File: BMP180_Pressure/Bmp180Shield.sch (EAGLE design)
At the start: 5 parts

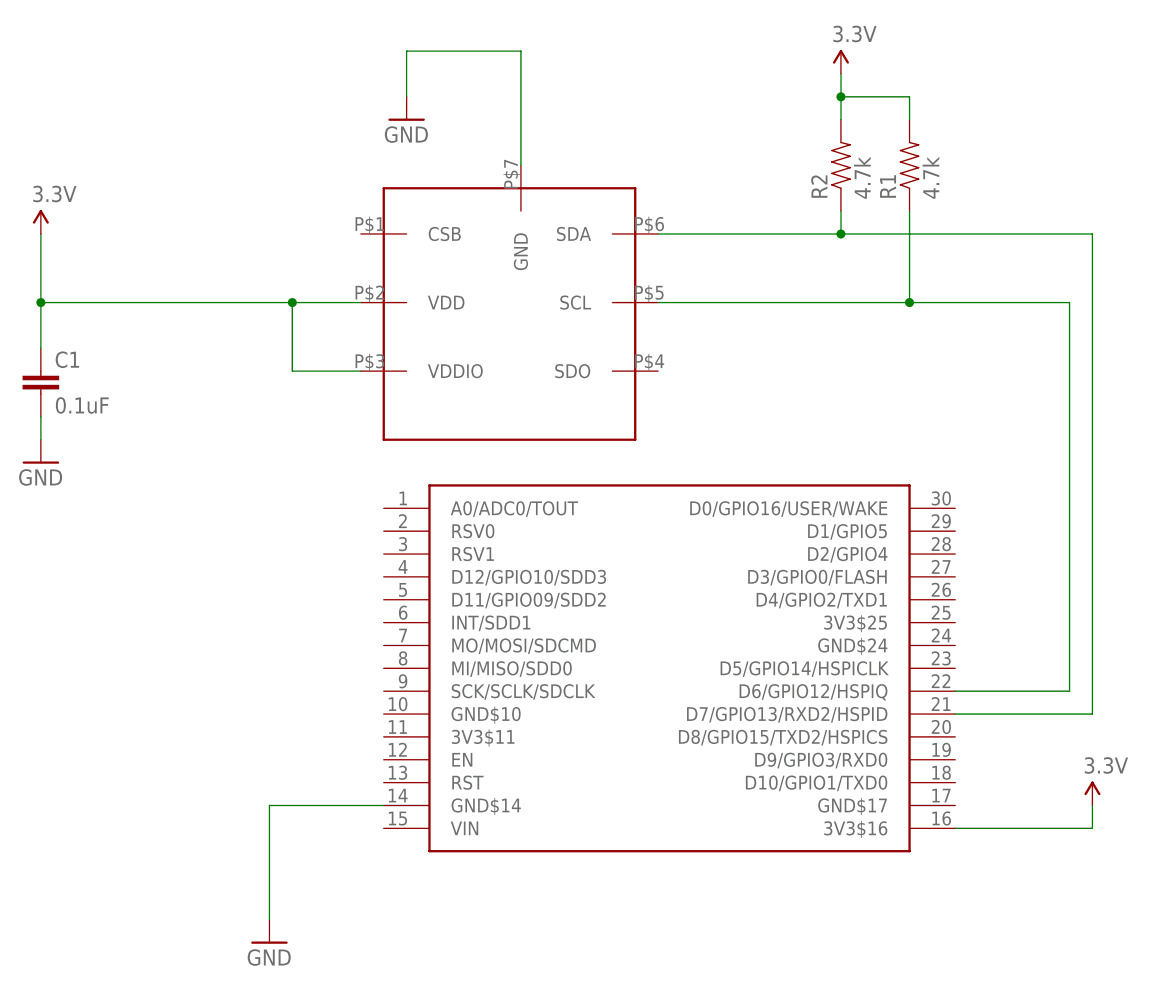
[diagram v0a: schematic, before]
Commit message: Updated BMP180 symbol Removed BMP085 shield (redundant) Added DS3231 RTC Shield Added LTC2495 ADC Shield Added chip data sheets for each shield
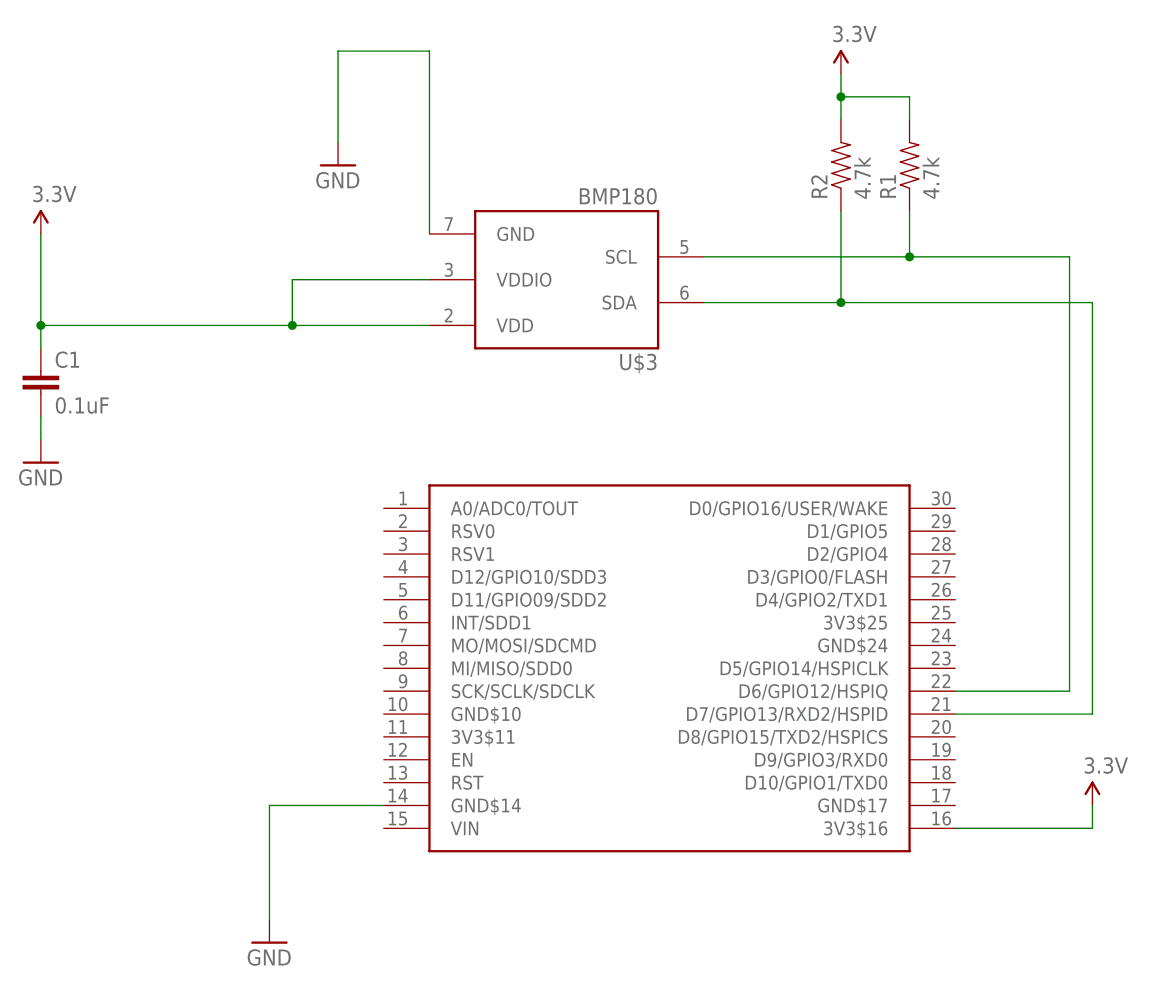
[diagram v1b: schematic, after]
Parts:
- U$3: device NerduinoShieldLib:BMP180 -> SparkFun-Sensors:BMP180
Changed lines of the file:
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@@
 <?xml version="1.0" encoding="utf-8"?>
 <!DOCTYPE eagle SYSTEM "eagle.dtd">
-<eagle version="7.3.0">
+<eagle version="7.4.0">
 <drawing>
 <settings>
@@
 <layer number="54" name="bGND_GNDA" color="1" fill="9" visible="no" active="no"/>
 <layer number="56" name="wert" color="7" fill="1" visible="no" active="no"/>
+<layer number="57" name="tCAD" color="7" fill="1" visible="no" active="no"/>
+<layer number="59" name="tCarbon" color="7" fill="1" visible="no" active="no"/>
+<layer number="60" name="bCarbon" color="7" fill="1" visible="no" active="no"/>
 <layer number="90" name="Modules" color="5" fill="1" visible="yes" active="yes"/>
 <layer number="91" name="Nets" color="2" fill="1" visible="yes" active="yes"/>
@@
 <layer number="97" name="Info" color="7" fill="1" visible="yes" active="yes"/>
 <layer number="98" name="Guide" color="6" fill="1" visible="yes" active="yes"/>
+<layer number="99" name="SpiceOrder" color="7" fill="1" visible="yes" active="yes"/>
 <layer number="100" name="Muster" color="7" fill="1" visible="no" active="no"/>
 <layer number="101" name="Patch_Top" color="12" fill="4" visible="yes" active="yes"/>
@@
 <layer number="106" name="bPlate" color="7" fill="1" visible="yes" active="yes"/>
 <layer number="107" name="Crop" color="7" fill="1" visible="yes" active="yes"/>
+<layer number="108" name="tplace-old" color="10" fill="1" visible="yes" active="yes"/>
+<layer number="109" name="ref-old" color="11" fill="1" visible="yes" active="yes"/>
+<layer number="110" name="fp0" color="7" fill="1" visible="yes" active="yes"/>
+<layer number="111" name="LPC17xx" color="7" fill="1" visible="yes" active="yes"/>
+<layer number="112" name="tSilk" color="7" fill="1" visible="yes" active="yes"/>
+<layer number="113" name="IDFDebug" color="7" fill="1" visible="yes" active="yes"/>
 <layer number="116" name="Patch_BOT" color="9" fill="4" visible="yes" active="yes"/>
+<layer number="118" name="Rect_Pads" color="7" fill="1" visible="yes" active="yes"/>
 <layer number="121" name="_tsilk" color="7" fill="1" visible="yes" active="yes"/>
 <layer number="122" name="_bsilk" color="7" fill="1" visible="yes" active="yes"/>
+<layer number="123" name="tTestmark" color="7" fill="1" visible="yes" active="yes"/>
+<layer number="124" name="bTestmark" color="7" fill="1" visible="yes" active="yes"/>
 <layer number="125" name="_tNames" color="7" fill="1" visible="yes" active="yes"/>
+<layer number="126" name="_bNames" color="7" fill="1" visible="yes" active="yes"/>
+<layer number="127" name="_tValues" color="7" fill="1" visible="yes" active="yes"/>
+<layer number="128" name="_bValues" color="7" fill="1" visible="yes" active="yes"/>
+<layer number="129" name="Mask" color="7" fill="1" visible="yes" active="yes"/>
+<layer number="131" name="tAdjust" color="7" fill="1" visible="yes" active="yes"/>
+<layer number="132" name="bAdjust" color="7" fill="1" visible="yes" active="yes"/>
 <layer number="144" name="Drill_legend" color="7" fill="1" visible="yes" active="yes"/>
+<layer number="150" name="Notes" color="7" fill="1" visible="yes" active="yes"/>
 <layer number="151" name="HeatSink" color="7" fill="1" visible="yes" active="yes"/>
+<layer number="152" name="_bDocu" color="7" fill="1" visible="yes" active="yes"/>
+<layer number="153" name="FabDoc1" color="7" fill="1" visible="yes" active="yes"/>
+<layer number="154" name="FabDoc2" color="7" fill="1" visible="yes" active="yes"/>
+<layer number="155" name="FabDoc3" color="7" fill="1" visible="yes" active="yes"/>
+<layer number="199" name="Contour" color="7" fill="1" visible="yes" active="yes"/>
 <layer number="200" name="200bmp" color="1" fill="10" visible="yes" active="yes"/>
 <layer number="201" name="201bmp" color="2" fill="10" visible="yes" active="yes"/>
@@
 <layer number="223" name="223bmp" color="24" fill="1" visible="no" active="no"/>
 <layer number="224" name="224bmp" color="25" fill="1" visible="no" active="no"/>
+<layer number="225" name="225bmp" color="7" fill="1" visible="yes" active="yes"/>
+<layer number="226" name="226bmp" color="7" fill="1" visible="yes" active="yes"/>
+<layer number="227" name="227bmp" color="7" fill="1" visible="yes" active="yes"/>
+<layer number="228" name="228bmp" color="7" fill="1" visible="yes" active="yes"/>
+<layer number="229" name="229bmp" color="7" fill="1" visible="yes" active="yes"/>
+<layer number="230" name="230bmp" color="7" fill="1" visible="yes" active="yes"/>
+<layer number="231" name="231bmp" color="7" fill="1" visible="yes" active="yes"/>
+<layer number="248" name="Housing" color="7" fill="1" visible="yes" active="yes"/>
+<layer number="249" name="Edge" color="7" fill="1" visible="yes" active="yes"/>
 <layer number="250" name="Descript" color="3" fill="1" visible="no" active="no"/>
 <layer number="251" name="SMDround" color="12" fill="11" visible="no" active="no"/>
 <layer number="254" name="cooling" color="7" fill="1" visible="yes" active="yes"/>
+<layer number="255" name="routoute" color="7" fill="1" visible="yes" active="yes"/>
 </layers>
 <schematic xreflabel="%F%N/%S.%C%R" xrefpart="/%S.%C%R">
@@
 <part name="C1" library="SparkFun" deviceset="CAP" device="0402-CAP" value="0.1uF"/>
 <part name="P+3" library="SparkFun" deviceset="3.3V" device=""/>
-<part name="U$3" library="NerduinoShieldLib" deviceset="BMP180" device=""/>
+<part name="U$3" library="SparkFun-Sensors" deviceset="BMP180" device=""/>
 <part name="GND3" library="SparkFun" deviceset="GND" device=""/>
 </parts>
@@
 <instance part="C1" gate="G$1" x="-30.48" y="78.74"/>
 <instance part="P+3" gate="G$1" x="58.42" y="114.3"/>
-<instance part="U$3" gate="G$1" x="7.62" y="101.6"/>
-<instance part="GND3" gate="1" x="10.16" y="109.22"/>
+<instance part="U$3" gate="G$1" x="27.94" y="91.44" rot="R180"/>
+<instance part="GND3" gate="1" x="2.54" y="104.14"/>
 </instances>
 <busses>
@@
 <segment>
 <pinref part="U$3" gate="G$1" pin="GND"/>
-<wire x1="22.86" y1="104.14" x2="22.86" y2="116.84" width="0.1524" layer="91"/>
+<wire x1="12.7" y1="96.52" x2="12.7" y2="116.84" width="0.1524" layer="91"/>
 <pinref part="GND3" gate="1" pin="GND"/>
-<wire x1="22.86" y1="116.84" x2="10.16" y2="116.84" width="0.1524" layer="91"/>
-<wire x1="10.16" y1="116.84" x2="10.16" y2="111.76" width="0.1524" layer="91"/>
+<wire x1="12.7" y1="116.84" x2="2.54" y2="116.84" width="0.1524" layer="91"/>
+<wire x1="2.54" y1="116.84" x2="2.54" y2="106.68" width="0.1524" layer="91"/>
 </segment>
 </net>
@@
 <segment>
 <pinref part="P+2" gate="G$1" pin="3.3V"/>
-<wire x1="-30.48" y1="88.9" x2="-30.48" y2="96.52" width="0.1524" layer="91"/>
-<junction x="-30.48" y="88.9"/>
+<wire x1="-30.48" y1="86.36" x2="-30.48" y2="96.52" width="0.1524" layer="91"/>
+<junction x="-30.48" y="86.36"/>
 <pinref part="C1" gate="G$1" pin="1"/>
-<wire x1="-30.48" y1="83.82" x2="-30.48" y2="88.9" width="0.1524" layer="91"/>
+<wire x1="-30.48" y1="83.82" x2="-30.48" y2="86.36" width="0.1524" layer="91"/>
 <pinref part="U$3" gate="G$1" pin="VDD"/>
-<wire x1="-30.48" y1="88.9" x2="-2.54" y2="88.9" width="0.1524" layer="91"/>
+<wire x1="-30.48" y1="86.36" x2="-2.54" y2="86.36" width="0.1524" layer="91"/>
 <pinref part="U$3" gate="G$1" pin="VDDIO"/>
-<wire x1="-2.54" y1="88.9" x2="5.08" y2="88.9" width="0.1524" layer="91"/>
-<wire x1="5.08" y1="81.28" x2="-2.54" y2="81.28" width="0.1524" layer="91"/>
-<wire x1="-2.54" y1="81.28" x2="-2.54" y2="88.9" width="0.1524" layer="91"/>
-<junction x="-2.54" y="88.9"/>
+<wire x1="-2.54" y1="86.36" x2="12.7" y2="86.36" width="0.1524" layer="91"/>
+<wire x1="12.7" y1="91.44" x2="-2.54" y2="91.44" width="0.1524" layer="91"/>
+<wire x1="-2.54" y1="91.44" x2="-2.54" y2="86.36" width="0.1524" layer="91"/>
+<junction x="-2.54" y="86.36"/>
 </segment>
 <segment>
@@
 <segment>
 <pinref part="R2" gate="G$1" pin="1"/>
-<wire x1="58.42" y1="96.52" x2="58.42" y2="99.06" width="0.1524" layer="91"/>
-<wire x1="58.42" y1="96.52" x2="86.36" y2="96.52" width="0.1524" layer="91"/>
-<wire x1="86.36" y1="96.52" x2="86.36" y2="43.18" width="0.1524" layer="91"/>
-<junction x="58.42" y="96.52"/>
+<wire x1="58.42" y1="88.9" x2="58.42" y2="99.06" width="0.1524" layer="91"/>
+<wire x1="58.42" y1="88.9" x2="86.36" y2="88.9" width="0.1524" layer="91"/>
+<wire x1="86.36" y1="88.9" x2="86.36" y2="43.18" width="0.1524" layer="91"/>
+<junction x="58.42" y="88.9"/>
 <pinref part="U$1" gate="G$1" pin="D7/GPIO13/RXD2/HSPID"/>
 <wire x1="86.36" y1="43.18" x2="71.12" y2="43.18" width="0.1524" layer="91"/>
 <pinref part="U$3" gate="G$1" pin="SDA"/>
-<wire x1="58.42" y1="96.52" x2="38.1" y2="96.52" width="0.1524" layer="91"/>
+<wire x1="58.42" y1="88.9" x2="43.18" y2="88.9" width="0.1524" layer="91"/>
 </segment>
 </net>
@@
 <segment>
 <pinref part="R1" gate="G$1" pin="1"/>
-<wire x1="66.04" y1="88.9" x2="66.04" y2="99.06" width="0.1524" layer="91"/>
-<wire x1="66.04" y1="88.9" x2="83.82" y2="88.9" width="0.1524" layer="91"/>
-<wire x1="83.82" y1="88.9" x2="83.82" y2="45.72" width="0.1524" layer="91"/>
+<wire x1="66.04" y1="93.98" x2="66.04" y2="99.06" width="0.1524" layer="91"/>
+<wire x1="66.04" y1="93.98" x2="83.82" y2="93.98" width="0.1524" layer="91"/>
+<wire x1="83.82" y1="93.98" x2="83.82" y2="45.72" width="0.1524" layer="91"/>
 <pinref part="U$1" gate="G$1" pin="D6/GPIO12/HSPIQ"/>
 <wire x1="83.82" y1="45.72" x2="71.12" y2="45.72" width="0.1524" layer="91"/>
 <pinref part="U$3" gate="G$1" pin="SCL"/>
-<wire x1="66.04" y1="88.9" x2="38.1" y2="88.9" width="0.1524" layer="91"/>
-<junction x="66.04" y="88.9"/>
-</segment>
-</net>
+<wire x1="66.04" y1="93.98" x2="43.18" y2="93.98" width="0.1524" layer="91"/>
+<junction x="66.04" y="93.98"/>
+</segment>
+</net>

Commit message: Added OLED Shield Added LiPo Battery Charger Shield Updated outlines of all shields to match the cutout of the nodemcu board
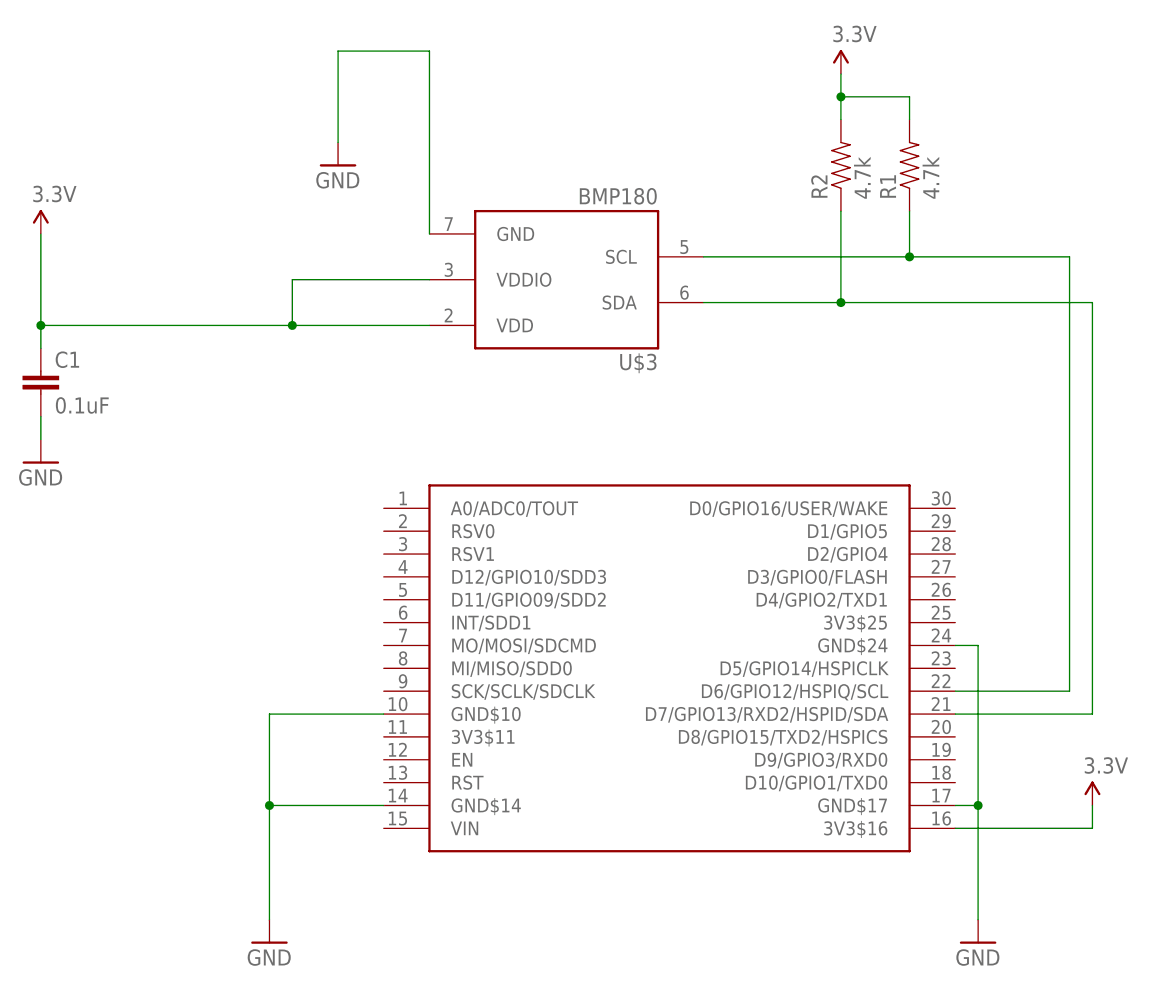
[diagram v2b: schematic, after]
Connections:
- net GND: now also U$1.GND$10, U$1.GND$17, U$1.GND$24
- net N$2: now also U$1.D7/GPIO13/RXD2/HSPID/SDA; no longer U$1.D7/GPIO13/RXD2/HSPID
- net N$3: now also U$1.D6/GPIO12/HSPIQ/SCL; no longer U$1.D6/GPIO12/HSPIQ
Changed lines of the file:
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@@
 <part name="U$3" library="SparkFun-Sensors" deviceset="BMP180" device=""/>
 <part name="GND3" library="SparkFun" deviceset="GND" device=""/>
+<part name="GND4" library="SparkFun" deviceset="GND" device=""/>
 </parts>
 <sheets>
@@
 <instance part="U$3" gate="G$1" x="27.94" y="91.44" rot="R180"/>
 <instance part="GND3" gate="1" x="2.54" y="104.14"/>
+<instance part="GND4" gate="1" x="73.66" y="17.78"/>
 </instances>
 <busses>
@@
 <wire x1="7.62" y1="33.02" x2="-5.08" y2="33.02" width="0.1524" layer="91"/>
 <wire x1="-5.08" y1="33.02" x2="-5.08" y2="20.32" width="0.1524" layer="91"/>
+<pinref part="U$1" gate="G$1" pin="GND$10"/>
+<wire x1="7.62" y1="43.18" x2="-5.08" y2="43.18" width="0.1524" layer="91"/>
+<wire x1="-5.08" y1="43.18" x2="-5.08" y2="33.02" width="0.1524" layer="91"/>
+<junction x="-5.08" y="33.02"/>
 </segment>
 <segment>
@@
 <wire x1="12.7" y1="116.84" x2="2.54" y2="116.84" width="0.1524" layer="91"/>
 <wire x1="2.54" y1="116.84" x2="2.54" y2="106.68" width="0.1524" layer="91"/>
+</segment>
+<segment>
+<pinref part="U$1" gate="G$1" pin="GND$17"/>
+<pinref part="GND4" gate="1" pin="GND"/>
+<wire x1="71.12" y1="33.02" x2="73.66" y2="33.02" width="0.1524" layer="91"/>
+<wire x1="73.66" y1="33.02" x2="73.66" y2="20.32" width="0.1524" layer="91"/>
+<pinref part="U$1" gate="G$1" pin="GND$24"/>
+<wire x1="71.12" y1="50.8" x2="73.66" y2="50.8" width="0.1524" layer="91"/>
+<wire x1="73.66" y1="50.8" x2="73.66" y2="33.02" width="0.1524" layer="91"/>
+<junction x="73.66" y="33.02"/>
 </segment>
 </net>
@@
 <wire x1="86.36" y1="88.9" x2="86.36" y2="43.18" width="0.1524" layer="91"/>
 <junction x="58.42" y="88.9"/>
-<pinref part="U$1" gate="G$1" pin="D7/GPIO13/RXD2/HSPID"/>
+<pinref part="U$1" gate="G$1" pin="D7/GPIO13/RXD2/HSPID/SDA"/>
 <wire x1="86.36" y1="43.18" x2="71.12" y2="43.18" width="0.1524" layer="91"/>
 <pinref part="U$3" gate="G$1" pin="SDA"/>
@@
 <wire x1="66.04" y1="93.98" x2="83.82" y2="93.98" width="0.1524" layer="91"/>
 <wire x1="83.82" y1="93.98" x2="83.82" y2="45.72" width="0.1524" layer="91"/>
-<pinref part="U$1" gate="G$1" pin="D6/GPIO12/HSPIQ"/>
+<pinref part="U$1" gate="G$1" pin="D6/GPIO12/HSPIQ/SCL"/>
 <wire x1="83.82" y1="45.72" x2="71.12" y2="45.72" width="0.1524" layer="91"/>
 <pinref part="U$3" gate="G$1" pin="SCL"/>
